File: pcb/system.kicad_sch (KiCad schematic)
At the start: 27 parts, among them J1 USB_C_Receptacle_USB2.0_16P, J2 Conn_01x04, U1 W25Q128JVS, U2 MB85RS1MT, U3 RP2040, Y1 ABM8-272-T3

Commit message: feat: finalized main system schematic
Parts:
- added BZ1: Buzzer, symbol Device:Buzzer
- added D1: LED, symbol Device:LED
- added R13, R14, R15: R, symbol Device:R
- added SW1, SW2: SW_Push, symbol Switch:SW_Push
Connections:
- net FLASH ~{CS} is gone; now on net +3.3V: U1.1 (~{CS}), U3.56 (QSPI_SS)
- net ~{RUN} is gone; now on net +3.3V: U3.26 (RUN)
- net +3.3V: now also SW1.1, SW2.1
- net GND: now also BZ1.2 (-), R13.2, R14.2, R15.2
- net BUZZER: now reaches U3.27 (GPIO16)
- net BUZZER: now also BZ1.1 (+)
- net HEARTBEAT: now reaches U3.37 (GPIO25)
- net HEARTBEAT: now also D1.2 (A)
- new net: D1.1 (K), R15.1
- new net: R14.1, SW2.2
- new net: R13.1, SW1.2
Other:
- note added: "Misc: Audiovisual indicators"
- note added: "Misc: Reset and Boot Selector Buttons"
- moved on the sheet: J2

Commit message: chore: page documentation
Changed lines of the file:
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@@
 	(title_block
 		(title "Banshee Microcontroller + Supporting Systems")
-		(date "2026-02-05")
+		(date "2026-02-18")
 		(rev "1")
 		(company "Ivan Leonard O Aparte <ivanleonard.aparte@cit.edu>")
+		(comment 1 "STEM 12 - Altruism | S.Y. 2025-2026")
 	)
 	(text "Special SPI interface for in-place execution.\nDoes not consume the two SPI controllers available\nas this one is a separate one for loading code\nn stuff"
@@
 					(unit 1)
 				)
-			)
-		)
-	)
-	(symbol
-		(lib_id "power:GND")
-		(at 264.16 160.02 270)
-		(mirror x)
-		(unit 1)
-		(exclude_from_sim no)
-		(in_bom yes)
-		(on_board yes)
-		(dnp no)
-		(fields_autoplaced yes)
-		(property "Reference" "#PWR044"
-			(at 257.81 160.02 0)
-			(effects
-				(font
-					(size 1.27 1.27)
-				)
-				(hide yes)
-			)
-		)
-		(property "Value" "GND"
-			(at 260.35 160.0199 90)
-			(effects
-				(font
-					(size 1.27 1.27)
-				)
-				(justify right)
-			)
-		)
-		(property "Footprint" ""
-			(at 264.16 160.02 0)
-			(effects
-				(font
-					(size 1.27 1.27)
-				)
-				(hide yes)
-			)
-		)
-		(property "Datasheet" ""
-			(at 264.16 160.02 0)
-			(effects
-				(font
-					(size 1.27 1.27)
-				)
-				(hide yes)
-			)
-		)
-		(property "Description" "Power symbol creates a global label with name \"GND\" , ground"
-			(at 264.16 160.02 0)
-			(effects
-				(font
-					(size 1.27 1.27)
-				)
-				(hide yes)
-			)
-		)
-		(pin "1"
-		)
-		(instances
-			(project ""
-				(path "/9bba97c2-2e09-46fb-bf2a-7de104403c7c/a98a71c0-d58c-4841-9b05-a84df7de5fc9"
-					(reference "#PWR044")
-					(unit 1)
-				)

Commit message: fix: reset wiring
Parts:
- added D2: LED, symbol Device:LED
- R14: value R -> 10k
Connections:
- net +3.3V: now also R14.1; no longer SW1.1, SW2.1, U1.1 (~{CS}), U3.26 (RUN), U3.56 (QSPI_SS)
- net GND: now also SW1.2, SW2.2; no longer R14.2
- net at R13.1: now also D2.1 (K); no longer SW1.2
- new net FLASH ~{CS}: R14.2, SW2.1, U1.1 (~{CS}), U3.56 (QSPI_SS)
- new net MCU ~{RESET}: SW1.1, U3.26 (RUN)
- new net VCC: D2.2 (A)
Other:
- note added: "FLASH ~{CS} pin is analogous to the ~{BOOTSEL} pin found in the RP Pico"
- moved on the sheet: D1, R14, R15, SW1, SW2

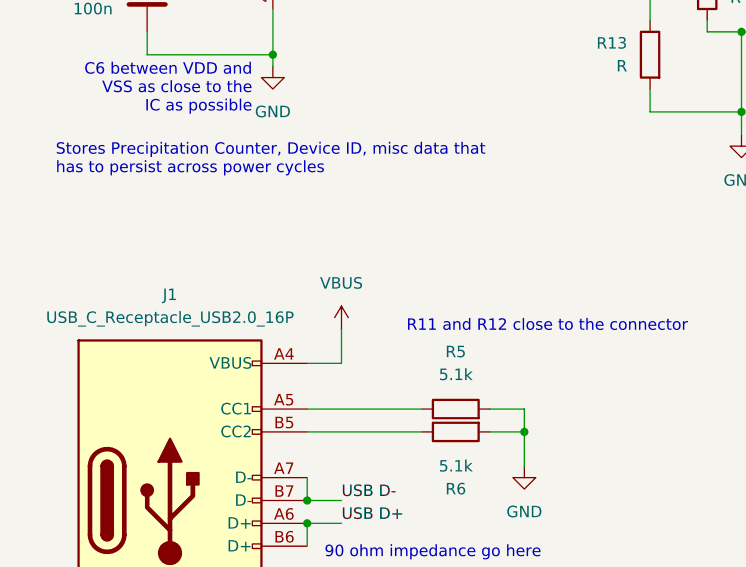
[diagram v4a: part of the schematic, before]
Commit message: feat: battery charging circuit
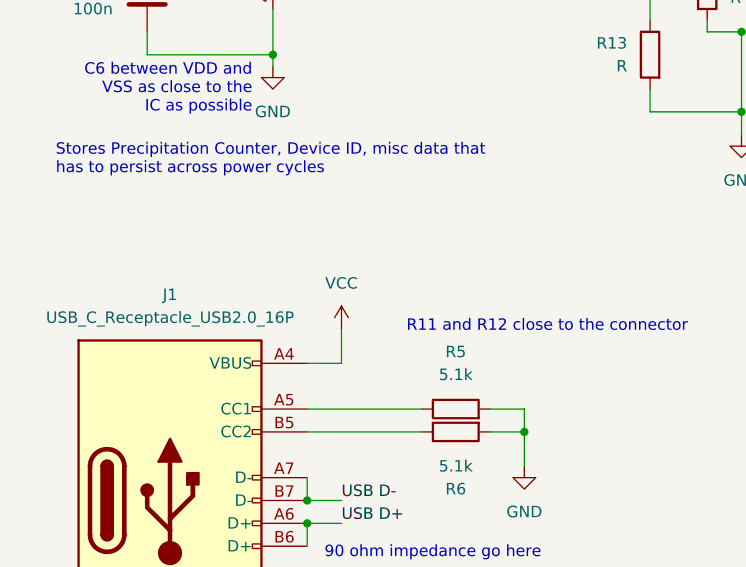
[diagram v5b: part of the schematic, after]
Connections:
- net VBUS is gone; now on net VCC: J1.A4 (VBUS), J1.A9 (VBUS), J1.B4 (VBUS), J1.B9 (VBUS)
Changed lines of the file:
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@@
 	)
 	(symbol
-		(lib_id "power:VBUS")
-		(at 52.07 140.97 0)
-		(unit 1)
-		(exclude_from_sim no)
-		(in_bom yes)
-		(on_board yes)
-		(dnp no)
-		(fields_autoplaced yes)
-		(property "Reference" "#PWR014"
-			(at 52.07 144.78 0)
-			(effects
-				(font
-					(size 1.27 1.27)
-				)
-				(hide yes)
-			)
-		)
-		(property "Value" "VBUS"
-			(at 52.07 135.89 0)
-			(effects
-				(font
-					(size 1.27 1.27)
-				)
-			)
-		)
-		(property "Footprint" ""
-			(at 52.07 140.97 0)
-			(effects
-				(font
-					(size 1.27 1.27)
-				)
-				(hide yes)
-			)
-		)
-		(property "Datasheet" ""
-			(at 52.07 140.97 0)
-			(effects
-				(font
-					(size 1.27 1.27)
-				)
-				(hide yes)
-			)
-		)
-		(property "Description" "Power symbol creates a global label with name \"VBUS\""
-			(at 52.07 140.97 0)
-			(effects
-				(font
-					(size 1.27 1.27)
-				)
-				(hide yes)
-			)
-		)
-		(pin "1"
-		)
-		(instances
-			(project ""
-				(path "/9bba97c2-2e09-46fb-bf2a-7de104403c7c/a98a71c0-d58c-4841-9b05-a84df7de5fc9"
-					(reference "#PWR014")
-					(unit 1)
-				)
-			)
-		)
-	)
-	(symbol
 		(lib_id "Device:LED")
 		(at 86.36 99.06 270)
@@
 					(unit 1)
 				)
+			)
+		)
+	)
+	(symbol
+		(lib_id "power:VCC")
+		(at 52.07 140.97 0)
+		(unit 1)
+		(exclude_from_sim no)
+		(in_bom yes)
+		(on_board yes)
+		(dnp no)
+		(fields_autoplaced yes)
+		(property "Reference" "#PWR070"
+			(at 52.07 144.78 0)
+			(effects
+				(font
+					(size 1.27 1.27)
+				)
+				(hide yes)
+			)
+		)
+		(property "Value" "VCC"
+			(at 52.07 135.89 0)
+			(effects
+				(font
+					(size 1.27 1.27)
+				)
+			)
+		)
+		(property "Footprint" ""
+			(at 52.07 140.97 0)
+			(effects
+				(font
+					(size 1.27 1.27)
+				)
+				(hide yes)
+			)
+		)
+		(property "Datasheet" ""
+			(at 52.07 140.97 0)
+			(effects
+				(font
+					(size 1.27 1.27)
+				)
+				(hide yes)
+			)
+		)
+		(property "Description" "Power symbol creates a global label with name \"VCC\""
+			(at 52.07 140.97 0)
+			(effects
+				(font
+					(size 1.27 1.27)
+				)
+				(hide yes)
+			)
+		)
+		(pin "1"
+		)
+		(instances
+			(project "pcb"
+				(path "/9bba97c2-2e09-46fb-bf2a-7de104403c7c/a98a71c0-d58c-4841-9b05-a84df7de5fc9"
+					(reference "#PWR070")
+					(unit 1)
+				)

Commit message: feat: wiring
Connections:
- net LOW BATTERY: now reaches U3.36 (GPIO24)
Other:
- note added: "SX1278 LoRa"
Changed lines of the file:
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@@
+		)
+	)
+	(text "SX1278 LoRa"
+		(exclude_from_sim no)
+		(at 223.52 100.584 0)
+		(effects
+			(font
+				(size 1.27 1.27)
+			)
 		)
 	)
@@
 	(wire
 		(pts
-			(xy 200.66 132.08) (xy 204.47 132.08)
+			(xy 200.66 132.08) (xy 219.71 132.08)
 		)
 		(stroke
@@
 		(pts
 			(xy 30.48 97.79) (xy 34.29 97.79)
+		)
+		(stroke
+			(width 0)
+			(type default)
+		)
+	)
+	(wire
+		(pts
+			(xy 200.66 129.54) (xy 204.47 129.54)
 		)
 		(stroke
@@
 	)
 	(label "HEARTBEAT"
-		(at 204.47 132.08 0)
+		(at 219.71 132.08 0)
 		(effects
 			(font
@@
 		(effects
 			(font
+				(size 1.27 1.27)
+			)
+			(justify left)
+		)
+	)
+	(hierarchical_label "LOW BATTERY"
+		(shape input)
+		(at 204.47 129.54 0)
+		(effects
+			(font

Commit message: feat: radio schematic
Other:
- title: Banshee Microcontroller + Supporting Systems -> Banshee Power Delivery System
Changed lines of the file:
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@@
 	(paper "A4")
 	(title_block
-		(title "Banshee Microcontroller + Supporting Systems")
-		(date "2026-02-18")
+		(title "Banshee Power Delivery System")
+		(date "2026-02-26")
 		(rev "1")
 		(company "Ivan Leonard O Aparte <ivanleonard.aparte@cit.edu>")

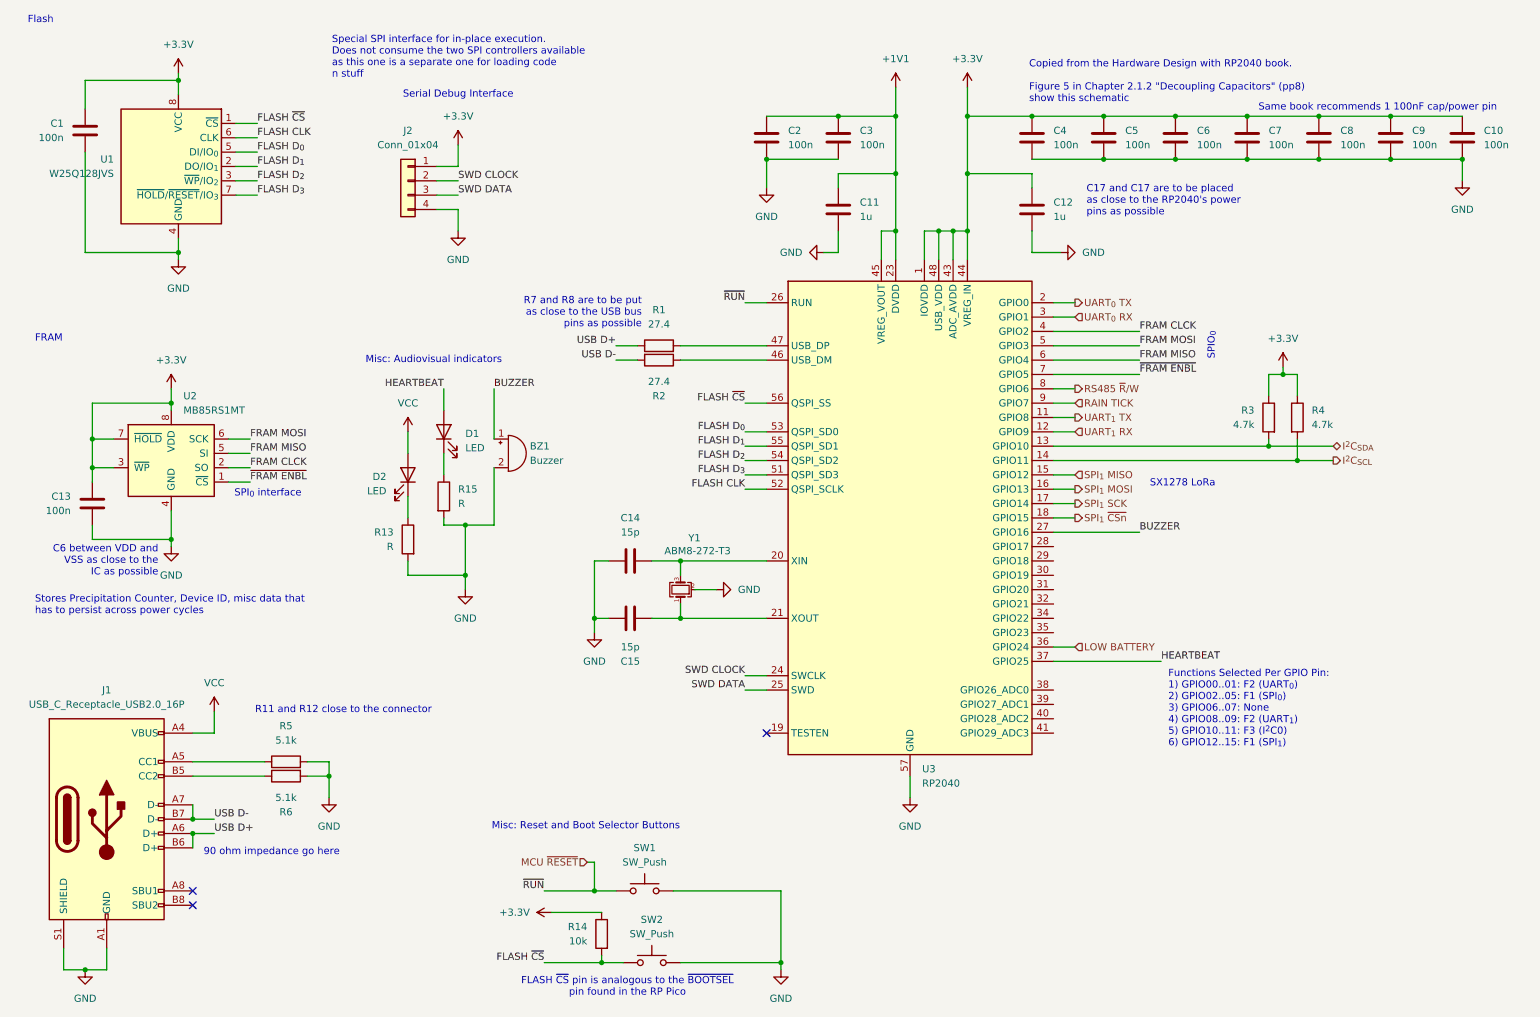
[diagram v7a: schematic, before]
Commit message: feat: revised 3.3v power rail, added power switch
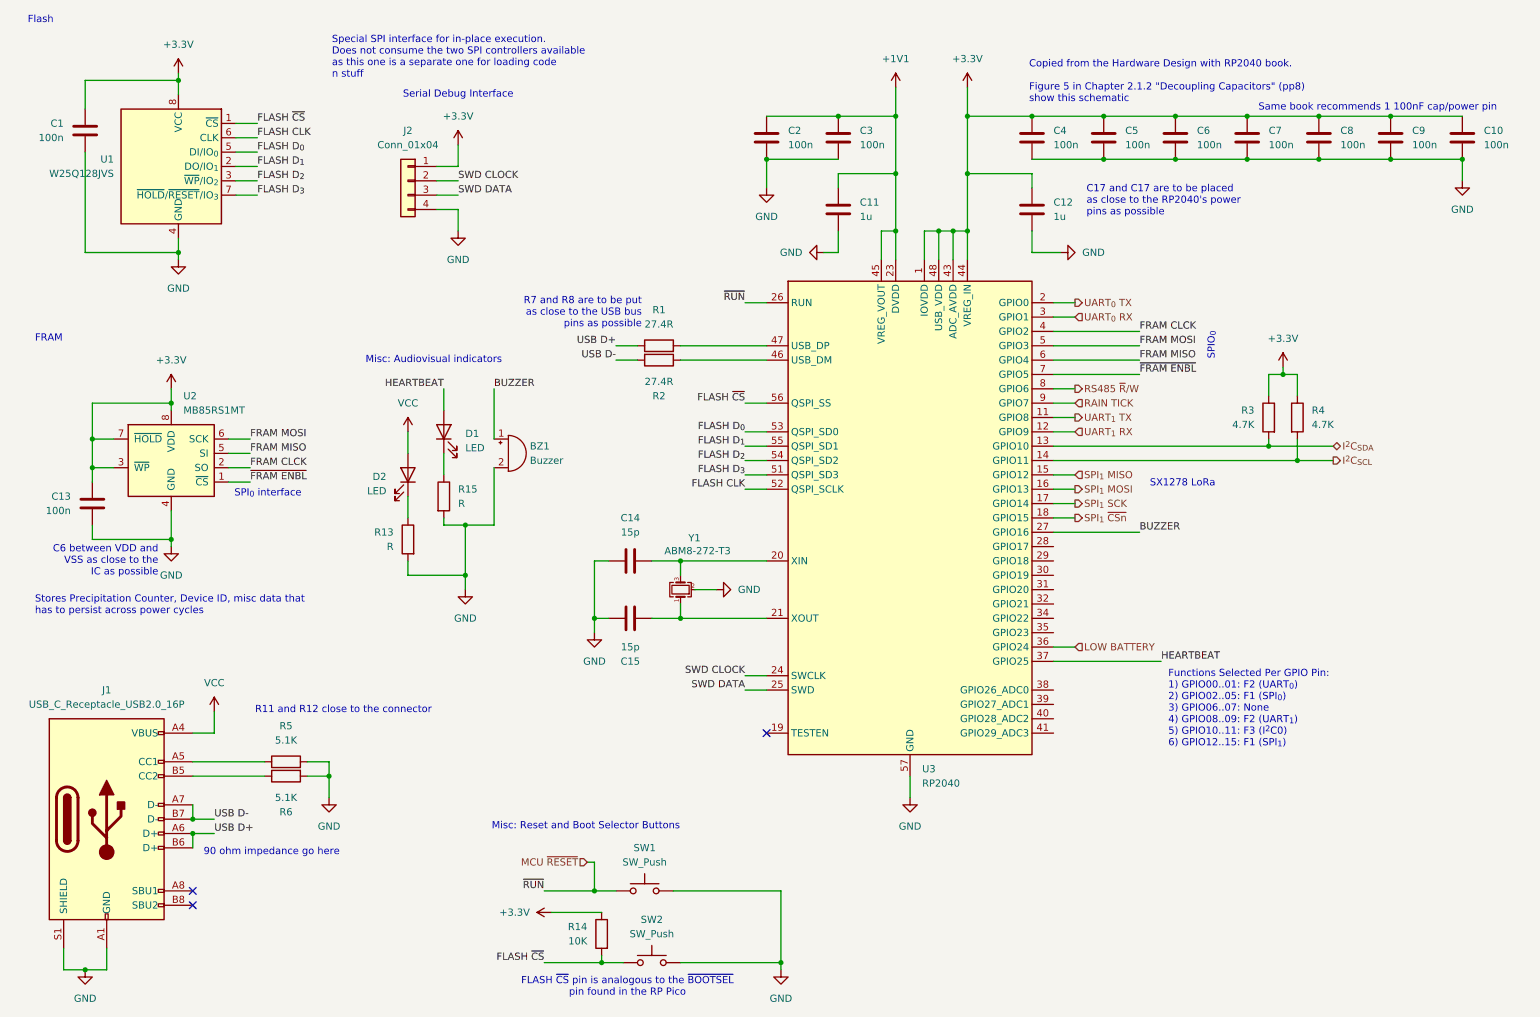
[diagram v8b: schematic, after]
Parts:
- R1, R2: value 27.4 -> 27.4R
- R14: value 10k -> 10K
- R3, R4: value 4.7k -> 4.7K
- R5, R6: value 5.1k -> 5.1K
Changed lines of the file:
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@@
 			)
 		)
-		(property "Value" "27.4"
+		(property "Value" "27.4R"
 			(at 130.81 82.55 90)
 			(effects
@@
 			)
 		)
-		(property "Value" "5.1k"
+		(property "Value" "5.1K"
 			(at 64.77 156.21 90)
 			(effects
@@
 			)
 		)
-		(property "Value" "10k"
+		(property "Value" "10K"
 			(at 118.11 181.6099 0)
 			(effects
@@
 			)
 		)
-		(property "Value" "4.7k"
+		(property "Value" "4.7K"
 			(at 236.22 90.1699 0)
 			(effects
@@
 			)
 		)
-		(property "Value" "27.4"
+		(property "Value" "27.4R"
 			(at 130.81 72.39 90)
 			(effects
@@
 			)
 		)
-		(property "Value" "5.1k"
+		(property "Value" "5.1K"
 			(at 64.77 146.05 90)
 			(effects
@@
 			)
 		)
-		(property "Value" "4.7k"
+		(property "Value" "4.7K"
 			(at 246.38 90.1699 0)
 			(effects
